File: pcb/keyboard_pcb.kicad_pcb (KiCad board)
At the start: 2 copper layers, 142.9 x 98.6 mm, 25 parts, among them J1 TRRS, K00 KEYSW, K01 KEYSW, K02 KEYSW, K03 KEYSW, K04 KEYSW, K05 KEYSW, K10 KEYSW, K11 KEYSW, K12 KEYSW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

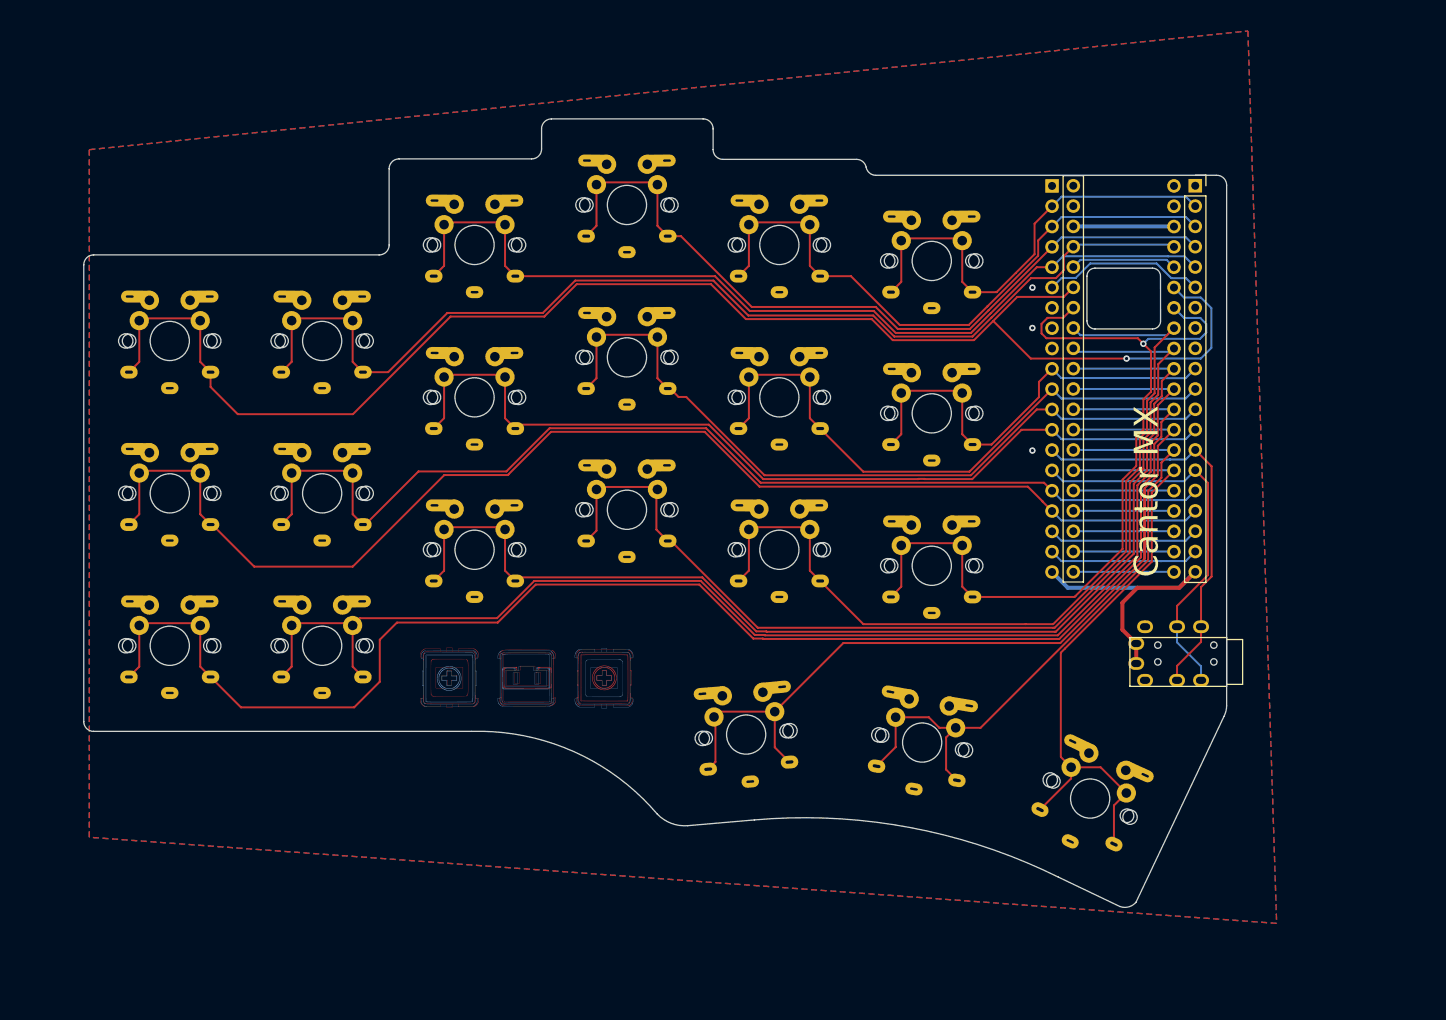
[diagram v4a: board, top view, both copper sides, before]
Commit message: Revised footprint for better Cherry MX 3-pin support Added teardrops Revised GND zone params to allow islands Removed unneeded island creating vias wiring tweaks
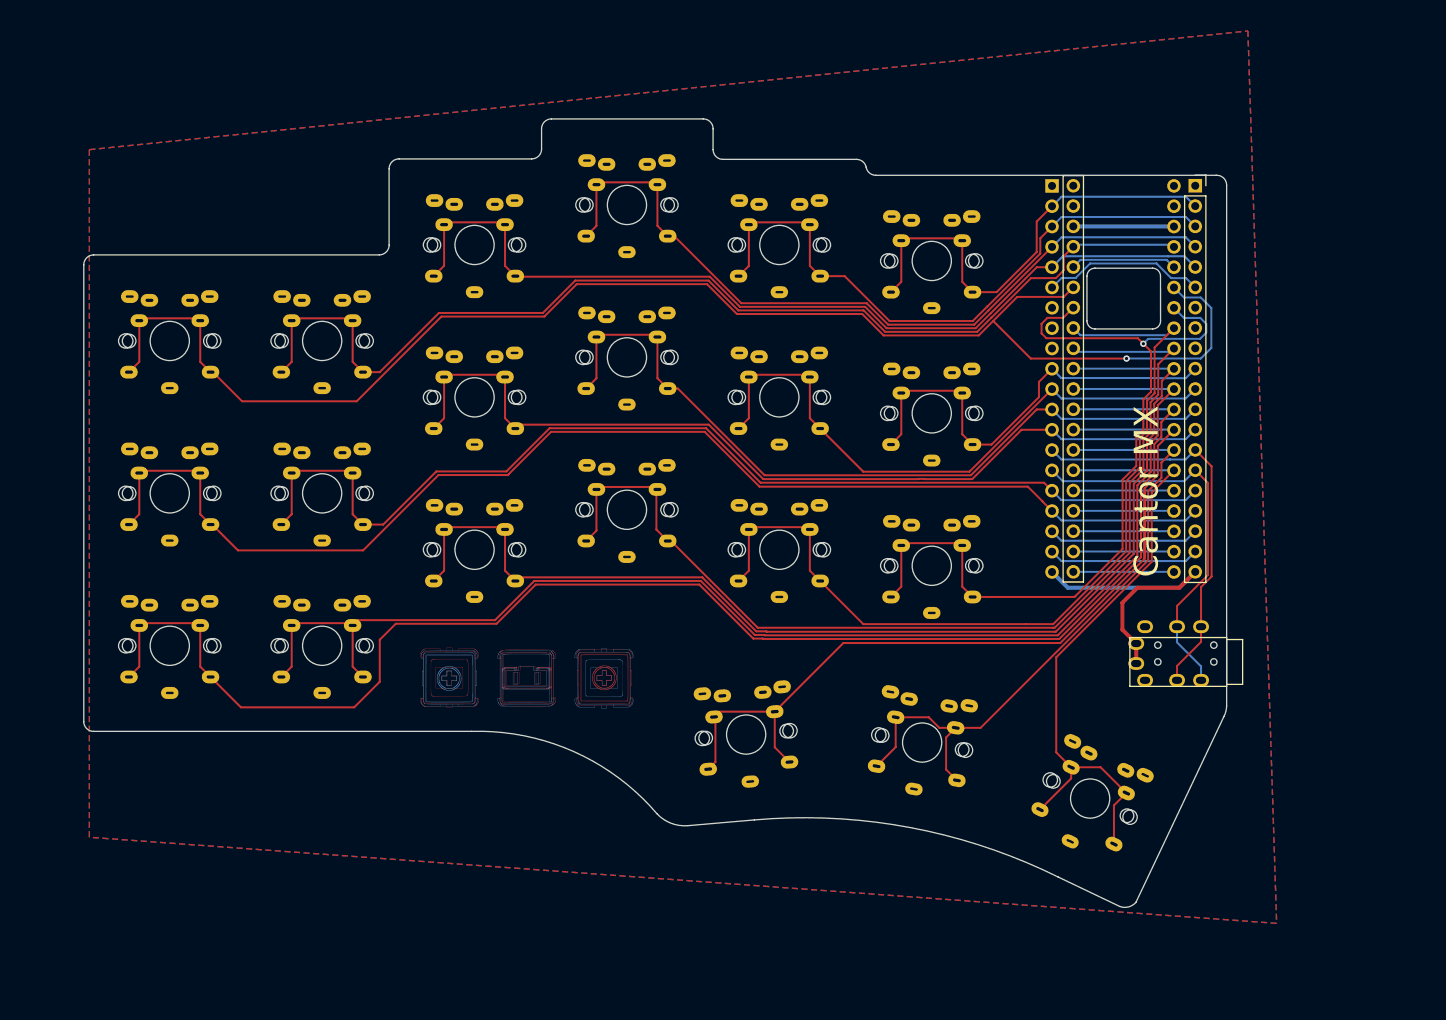
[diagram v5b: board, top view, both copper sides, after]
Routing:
- net /k00: track 185.0 -> 182.0 mm
- net /k10: track 158.2 -> 156.5 mm
- net GND: vias 3 -> 0
